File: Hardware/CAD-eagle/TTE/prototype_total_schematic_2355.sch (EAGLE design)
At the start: 32 parts, among them J2 MOLEX_48037-0001MOLEX_48037-0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, J4 RX

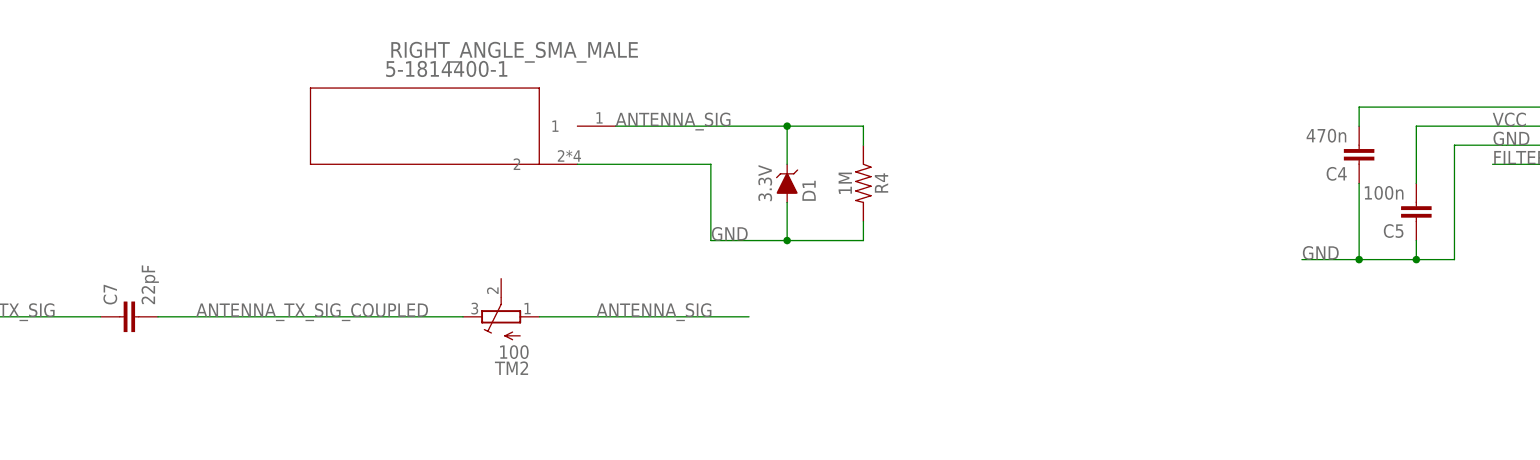
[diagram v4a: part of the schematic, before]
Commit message: Reciever Pipeline Confirmed, Updated Gerbers, included tx coupling capacitor for rx offset
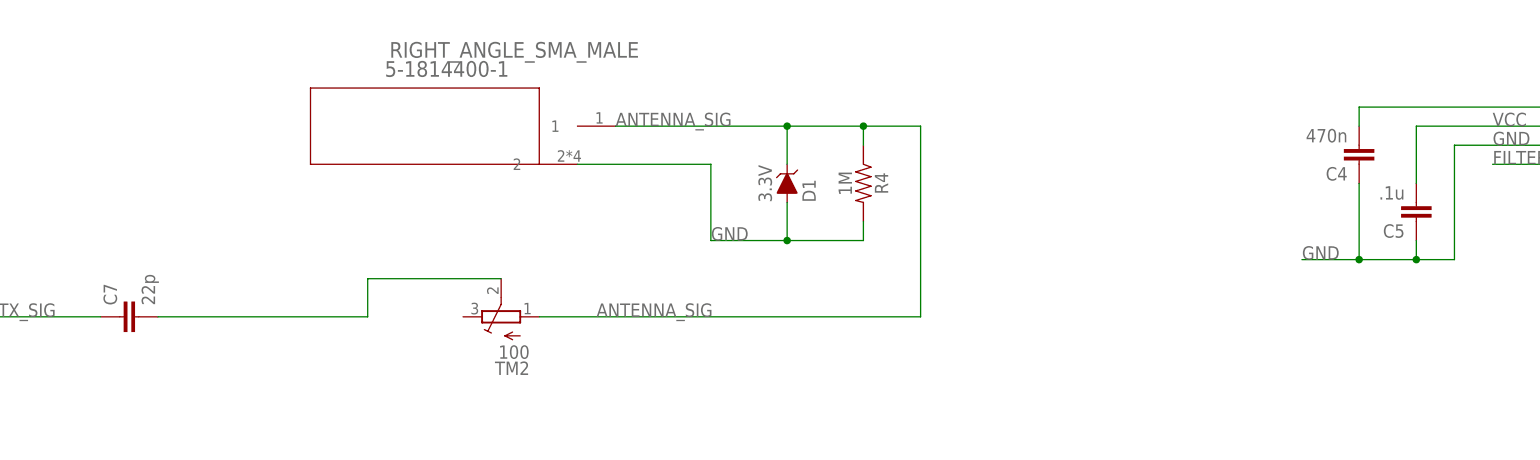
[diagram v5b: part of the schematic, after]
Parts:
- C5: value 100n -> .1u
- C7: value 22pF -> 22p
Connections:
- removed net ANTENNA_TX_SIG_COUPLED: C7.2, TM2.E
- new net N$2: C7.2, TM2.S
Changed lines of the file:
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@@
 <part name="TL069" library="TTE" deviceset="LTC1069-7CS8#PBF" device=""/>
 <part name="C4" library="SparkFun-Capacitors" deviceset="22UF" device="-0805-6.3V-20%" value="470n"/>
-<part name="C5" library="SparkFun-Capacitors" deviceset="22UF" device="-0805-6.3V-20%" value="100n"/>
+<part name="C5" library="SparkFun-Capacitors" deviceset="22UF" device="-0805-6.3V-20%" value=".1u"/>
 <part name="1K" library="microbuilder" deviceset="RESISTOR" device="0805" value="1k"/>
 <part name="47K" library="microbuilder" deviceset="RESISTOR" device="0805" value="47k"/>
@@
 <part name="VCC" library="SparkFun-Connectors" deviceset="CONN_04" device="" value="455-1750-1-ND"/>
 <part name="GND" library="SparkFun-Connectors" deviceset="CONN_04" device="" value="455-1750-1-ND"/>
-<part name="C7" library="SparkFun-Capacitors" deviceset="22UF" device="-0805-6.3V-20%" value="22pF"/>
+<part name="C7" library="SparkFun-Capacitors" deviceset="22UF" device="-0805-6.3V-20%" value="22p"/>
 </parts>
 <sheets>
@@
 <net name="ANTENNA_SIG" class="0">
 <segment>
+<pinref part="TM2" gate="G$1" pin="A"/>
+<wire x1="-154.94" y1="35.56" x2="-104.14" y2="35.56" width="0.1524" layer="91"/>
+<label x="-147.32" y="35.56" size="1.778" layer="95"/>
+<wire x1="-104.14" y1="35.56" x2="-104.14" y2="60.96" width="0.1524" layer="91"/>
 <pinref part="RIGHT_ANGLE_SMA_MALE" gate="A" pin="1"/>
 <label x="-144.78" y="60.96" size="1.778" layer="95"/>
@@
 <wire x1="-121.92" y1="60.96" x2="-111.76" y2="60.96" width="0.1524" layer="91"/>
 <wire x1="-111.76" y1="60.96" x2="-111.76" y2="58.42" width="0.1524" layer="91"/>
-</segment>
-<segment>
-<pinref part="TM2" gate="G$1" pin="A"/>
-<wire x1="-154.94" y1="35.56" x2="-127" y2="35.56" width="0.1524" layer="91"/>
-<label x="-147.32" y="35.56" size="1.778" layer="95"/>
+<wire x1="-104.14" y1="60.96" x2="-111.76" y2="60.96" width="0.1524" layer="91"/>
+<junction x="-111.76" y="60.96"/>
 </segment>
 <segment>
@@
 </segment>
 </net>
-<net name="ANTENNA_TX_SIG_COUPLED" class="0">
-<segment>
-<label x="-200.66" y="35.56" size="1.778" layer="95"/>
-<pinref part="TM2" gate="G$1" pin="E"/>
+<net name="N$2" class="0">
+<segment>
 <pinref part="C7" gate="G$1" pin="2"/>
-<wire x1="-205.74" y1="35.56" x2="-165.1" y2="35.56" width="0.1524" layer="91"/>
-</segment>
-</net>
+<wire x1="-205.74" y1="35.56" x2="-177.8" y2="35.56" width="0.1524" layer="91"/>
+<wire x1="-177.8" y1="35.56" x2="-177.8" y2="40.64" width="0.1524" layer="91"/>
+<pinref part="TM2" gate="G$1" pin="S"/>
+<wire x1="-177.8" y1="40.64" x2="-160.02" y2="40.64" width="0.1524" layer="91"/>
+</segment>
+</net>

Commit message: MODEM Files
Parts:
- removed FILT: FILT, SparkFun-Connectors:CONN_02
- removed GND, RXD, TCK, TDIO, TXD, VCC: 455-1750-1-ND, SparkFun-Connectors:CONN_04
- removed J4, SIG: RX, SparkFun-Connectors:CONN_02
- removed RIGHT_ANGLE_SMA_MALE: 5-1814400-1, TTE:5-1814400-1
- removed RST: MOMENTARY-SWITCH-SPST-PTH-6.0MM, SparkFun-Switches:MOMENTARY-SWITCH-SPST-PTH-6.0MM
- added J: 0, SparkFun-Resistors:2.0KOHM-0603-1/10W-5%
- added J1: (no value), SparkFun-Connectors:CONN_07NO_SILK
- added RESET: MOMENTARY-SWITCH-SPST-PTH-6.0MM, SparkFun-Switches:MOMENTARY-SWITCH-SPST-PTH-6.0MM
- added U$1: USB-PCB, TTE:USB-PCB
- added _: 5-1814400-1, TTE:5-1814400-1
- C2: value 100nF -> 22p
- C7: value 22p -> 100nF
- renumbered MSP430 to MSP430FR2355
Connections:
- removed net ADC: J4.2, MSP430FR2355.P1.1/UCB0CLK/ACLK/OA0O/COMP0.1/A1, MSP430FR2355.P1.2/UCB0SIMO/UCB0SDA/TB0TRG/OA0-/A2/VEREF
- removed net BCLUART_RXD_EXT: RXD.3, RXD.4
- removed net BCLUART_RXD_USB: FT232RL.TXD, RXD.1
- removed net BCLUART_TXD_EXT: TXD.3, TXD.4
- removed net BCLUART_TXD_USB: FT232RL.RXD, TXD.1
- removed net GND_EXT: GND.3, GND.4
- removed net GND_USB: GND.1
- removed net RST/SBWTDIO_EXT: TDIO.3, TDIO.4
- removed net RST/SBWTDIO_USB: FT232RL.DTR, TDIO.1
- removed net RX_PGA_1: J4.1, MSP430FR2355.P1.3/UCB0SOMI/UCB0SCL/OA0+/A3, MSP430FR2355.P3.1/OA2O
- removed net TEST/SSBWTCK_USB: FT232RL.RTS, TCK.1
- removed net TST/SBWTCK_EXT: TCK.3, TCK.4
- removed net VCC_EXT: VCC.3, VCC.4
- removed net VCC_USB: FT232RL.3V3OUT, FT232RL.VCCIO, VCC.1
- new net NC_5V: J1.6
- new net RX: FT232RL.TXD, MSP430FR2355.P1.6/UCA0RXD/UCA0SOMI/TB0.1/TDI/TCLK/OA1-/A6
- new net RX_PGA_2: MSP430FR2355.P1.1/UCB0CLK/ACLK/OA0O/COMP0.1/A1, MSP430FR2355.P5.0/TB2.1/MFM.RX/A8
- new net TX: FT232RL.RXD, MSP430FR2355.P1.7/UCA0TXD/UCA0SIMO/TB0.2/TDO/OA1+/A7/VREF+
- net ANTENNA_SIG: now also J.2, TM2.E, _.1; no longer RIGHT_ANGLE_SMA_MALE.1, SIG.1, TM2.A
- net ANTENNA_TX_SIG: now also J.1, TM2.S; no longer C7.1, SIG.2
- net BCLUART_RXD: now also J1.4; no longer MSP430FR2355.P1.6/UCA0RXD/UCA0SOMI/TB0.1/TDI/TCLK/OA1-/A6, RXD.2
- net BCLUART_TXD: now also J1.3; no longer MSP430FR2355.P1.7/UCA0TXD/UCA0SIMO/TB0.2/TDO/OA1+/A7/VREF+, TXD.2
- net FILTER_IN: now also MSP430FR2355.P5.1/TB2.2/MFM.TX/A9; no longer FILT.2, MSP430FR2355.P5.0/TB2.1/MFM.RX/A8
- net FILTER_OUT: no longer FILT.1
- net GND: now also C2.1, C7.2, J1.7, RESET.1, U$1.GND; no longer C2.2, GND.2, RIGHT_ANGLE_SMA_MALE.2, RST.1
- net N$2: now also C2.2, _.2; no longer C7.2, TM2.S
- net RST/SBWTDIO: now also J1.2, RESET.2; no longer RST.2, TDIO.2
- net STATUS_LED: now also MSP430FR2355.P4.7/UCB1SOMI/UCB1SCL; no longer MSP430FR2355.P2.5/COMP1.0
- net TEST/SSBWTCK: now also J1.1; no longer TCK.2
- net USB_DATA_+: now also J2.3, U$1.D+; no longer J2.2
- net USB_DATA_-: now also J2.2, U$1.D-; no longer J2.3
- net VCC: now also FT232RL.3V3OUT, FT232RL.VCCIO, J1.5; no longer C2.1, VCC.2
- net V_USB: now also C7.1, U$1.VCC
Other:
- note added: "Connect to msp430 evm Programs via spi-bi wire"
- note added: "Programming"
- note added: "Square Wave / PWM DAC"
- note added: "[ ] denotes internal connection Full duplex: rx: SAC 2 [-> SAC 0 -> ADC ] tx: SAC 1 -> filt -> SAC 3 -> out TDD: rx: SAC 2 -> SAC 1 -> filt -> [SAC 0 -> ADC] tx: SAC 1 -> filt -> SAC 3 -> OUT ADC is A1"
- note removed: "Couple headers for good measure"
- note removed: "Debugging"
- moved on the sheet: C2, C7, D1, R2, R4, STATUS, TM2

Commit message: V3 PCB schematics Ordered
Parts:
- removed J: 0, SparkFun-Resistors:2.0KOHM-0603-1/10W-5%
- removed MSP430FR2355: MSP430FR2355, TTE:MSP430FR2355
- added FILTER: (no value), microbuilder:HEADER-1X2ROUND
- added MSPFR2355-DBT: MSPFR2355-DBT, TTE:MSPFR2355-DBT
- C1: value 10µF -> 10u
- C3: value 22uF -> 22u
- C7: value 100nF -> 100n
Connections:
- net ANTENNA_SIG: now also MSPFR2355-DBT.P3.3/OA2+; no longer J.2, MSP430FR2355.P3.3/OA2+
- net ANTENNA_TX_SIG: now also MSPFR2355-DBT.P3.5/OA3O; no longer J.1, MSP430FR2355.P3.5/OA3O
- net BCLUART_RXD: now also MSPFR2355-DBT.P4.2/UCA1RXD/UCA1SOMI/UCA1RXD; no longer MSP430FR2355.P4.2/UCA1RXD/UCA1SOMI/UCA1RXD
- net BCLUART_TXD: now also MSPFR2355-DBT.P4.3/UCA1TXD/UCA1SIMO/UCA1TXD; no longer MSP430FR2355.P4.3/UCA1TXD/UCA1SIMO/UCA1TXD
- net FILTER_CLK: now also MSPFR2355-DBT.P2.1/TB1.2/COMP1.O; no longer MSP430FR2355.P2.1/TB1.2/COMP1.O
- net FILTER_IN: now also FILTER.2, MSPFR2355-DBT.P1.5/UCA0CLK/TMS/OA1O/A5; no longer MSP430FR2355.P1.5/UCA0CLK/TMS/OA1O/A5, MSP430FR2355.P5.1/TB2.2/MFM.TX/A9
- net FILTER_OUT: now also FILTER.1, MSPFR2355-DBT.P3.7/OA3+, MSPFR2355-DBT.P5.1/TB2.2/MFM.TX/A9; no longer MSP430FR2355.P3.7/OA3+
- net GND: now also MSPFR2355-DBT.DVSS; no longer J2.MNT_1, J2.MNT_2, MSP430FR2355.DVSS
- net RST/SBWTDIO: now also MSPFR2355-DBT.RST/NMI/SBWTDIO; no longer MSP430FR2355.RST/NMI/SBWTDIO
- net RX: now also MSPFR2355-DBT.P1.6/UCA0RXD/UCA0SOMI/TB0.1/TDI/TCLK/OA1-/A6; no longer MSP430FR2355.P1.6/UCA0RXD/UCA0SOMI/TB0.1/TDI/TCLK/OA1-/A6
- net RX_PGA_2: now also MSPFR2355-DBT.P1.1/UCB0CLK/ACLK/OA0O/COMP0.1/A1, MSPFR2355-DBT.P5.0/TB2.1/MFM.RX/A8; no longer MSP430FR2355.P1.1/UCB0CLK/ACLK/OA0O/COMP0.1/A1, MSP430FR2355.P5.0/TB2.1/MFM.RX/A8
- net STATUS_LED: now also MSPFR2355-DBT.P4.7/UCB1SOMI/UCB1SCL; no longer MSP430FR2355.P4.7/UCB1SOMI/UCB1SCL
- net TEST/SSBWTCK: now also MSPFR2355-DBT.TEST/SBWTCK; no longer MSP430FR2355.TEST/SBWTCK
- net TX: now also MSPFR2355-DBT.P1.7/UCA0TXD/UCA0SIMO/TB0.2/TDO/OA1+/A7/VREF+; no longer MSP430FR2355.P1.7/UCA0TXD/UCA0SIMO/TB0.2/TDO/OA1+/A7/VREF+
- net VCC: now also MSPFR2355-DBT.DVCC; no longer MSP430FR2355.DVCC
